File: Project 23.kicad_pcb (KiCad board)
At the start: 2 copper layers, 62 x 42 mm, 47 parts, among them J11 SRX 1, J12 SRX 2, J13 SWD, J21 Batt, J61 USB_Micro, M2 Hole_M2, Q51 Si2315, SW11 UI_Btn, SW12 PWR_BTN, U1 STM32F103C8T7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

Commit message: Completed V0.7 PCB Design
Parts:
- removed 1, M2: Hole_M2, MountingHole:MountingHole_2.2mm_M2
- removed Q51: Si2315, Package_TO_SOT_SMD:SOT-23_Handsoldering
- removed R51, R64: 10k, Resistor_SMD:R_0805_2012Metric_Pad1.15x1.40mm_HandSolder
- removed U2: MCP73811, Package_TO_SOT_SMD:SOT-23-5_HandSoldering
- removed U3: NCP551, Package_TO_SOT_SMD:SOT-23-5_HandSoldering
- removed U4: NCP1402, Package_TO_SOT_SMD:SOT-23-5_HandSoldering
- added C33: 1uF, Capacitor_SMD:C_0805_2012Metric_Pad1.15x1.40mm_HandSolder, F.Cu at (87.4, 42.7)
- added C34: 1uF, Capacitor_SMD:C_0805_2012Metric_Pad1.15x1.40mm_HandSolder, F.Cu at (80.3, 42.7)
- added C71: 1uF, Capacitor_SMD:C_0805_2012Metric_Pad1.15x1.40mm_HandSolder, F.Cu at (91.4, 62.0)
- added D11: MMBD1205, Package_TO_SOT_SMD:SOT-23, F.Cu at (79.2, 62.0)
- added H1: M2, MountingHole:MountingHole_2.2mm_M2, F.Cu at (55.8, 42.0)
- added H2: M2, MountingHole:MountingHole_2.2mm_M2, F.Cu at (64.0, 79.5)
- added H3: M2, MountingHole:MountingHole_2.2mm_M2, F.Cu at (107.8, 79.2)
- added H4: M2, MountingHole:MountingHole_2.2mm_M2, F.Cu at (107.8, 45.5)
- added J22: BATT-, Connector_PinHeader_2.54mm:PinHeader_1x01_P2.54mm_Vertical, F.Cu at (59.7, 41.9)
- added J71: Micro_SD_Card_Det, Project 23:micro sd holder, F.Cu at (108.0, 61.0)
- added R15: 10k, Resistor_SMD:R_0805_2012Metric_Pad1.15x1.40mm_HandSolder, F.Cu at (80.3, 66.3)
- added R16: 10k, Resistor_SMD:R_0805_2012Metric_Pad1.15x1.40mm_HandSolder, F.Cu at (78.2, 66.3)
- added R21: 10k, Resistor_SMD:R_0805_2012Metric_Pad1.15x1.40mm_HandSolder, F.Cu at (55.4, 47.8)
- added R22: 10k, Resistor_SMD:R_0805_2012Metric_Pad1.15x1.40mm_HandSolder, F.Cu at (62.5, 45.2)
- added R81: 10k, Resistor_SMD:R_0805_2012Metric_Pad1.15x1.40mm_HandSolder, F.Cu at (59.2, 49.0)
- added R82: 10k, Resistor_SMD:R_0805_2012Metric_Pad1.15x1.40mm_HandSolder, F.Cu at (61.2, 49.0)
- added R83: 10k, Resistor_SMD:R_0805_2012Metric_Pad1.15x1.40mm_HandSolder, F.Cu at (65.3, 49.0)
- added R84: 10k, Resistor_SMD:R_0805_2012Metric_Pad1.15x1.40mm_HandSolder, F.Cu at (63.2, 49.0)
- added TP31: 3V3SB, TestPoint:TestPoint_Pad_D2.0mm, F.Cu at (79.8, 80.2)
- added TP32: 3V3, TestPoint:TestPoint_Pad_D2.0mm, F.Cu at (77.0, 80.2)
- added TP41: 5V, TestPoint:TestPoint_Pad_D2.0mm, F.Cu at (82.5, 80.2)
- added TP75: GND, TestPoint:TestPoint_Pad_D2.0mm, F.Cu at (85.2, 80.0)
- added U21: MCP73832, Package_TO_SOT_SMD:SOT-23-5_HandSoldering, F.Cu at (55.4, 45.2)
- added U31: NCP551, Package_TO_SOT_SMD:SOT-23-5_HandSoldering, F.Cu at (83.8, 46.7)
- added U32: MIC5504, Package_TO_SOT_SMD:SOT-23-5_HandSoldering, F.Cu at (83.8, 42.7)
- added U41: NCP1402, Package_TO_SOT_SMD:SOT-23-5_HandSoldering, F.Cu at (87.2, 71.4)
- J21: value Batt -> BATT +; footprint Connector_PinHeader_2.54mm:PinHeader_1x02_P2.54mm_Vertical -> Connector_PinHeader_2.54mm:PinHeader_1x01_P2.54mm_Vertical
- J61: footprint Project 23:usbMicro -> Project 23:microUsbSunken
- moved C31 32.1 mm to (87.4, 46.7), turned to 270 degrees
- moved C32 24.3 mm to (80.3, 46.7), turned to 90 degrees
- moved C16 19.3 mm to (70.1, 47.2), turned to 0 degrees
- moved C41 16.8 mm to (79.5, 71.0)
- moved RN1 15.6 mm to (83.8, 63.2), turned to 0 degrees
- moved C19 14.6 mm to (75.9, 58.9), turned to 270 degrees
- moved C42 11.3 mm to (93.3, 76.8), turned to 270 degrees
- moved L41 9.51 mm to (82.8, 70.9)
- moved F12 9.04 mm to (78.0, 74.5), turned to 0 degrees
- moved C11 8.35 mm to (84.1, 54.9), turned to 270 degrees
- moved R63 8.19 mm to (60.7, 57.5), turned to 180 degrees
- moved U1 7.93 mm to (71.8, 53.6)
- moved C21 7.47 mm to (58.9, 45.2), turned to 90 degrees
- moved C18 7.37 mm to (66.3, 57.9), turned to 180 degrees
- moved D41 7.32 mm to (88.9, 68.1), turned to 180 degrees
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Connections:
- C16 pad 1: +3V3 -> /3V3SB
- C17 pad 1: +3V3 -> /3V3SB
- C18 pad 1: +3V3 -> /3V3SB
- C19 pad 1: +3V3 -> /3V3SB
- C21 pad 1: +BATT -> VBUS
- C22 pad 1: VBUS -> +BATT
- C32 pad 1: +3V3 -> /3V3SB
- R41 pad 1: /Boost_En -> /PWR_EN
- R63 pad 2: /USB_PU -> +3V3
- RN12 pad 3: (no net) -> Net-(J11-Pad6)
- RN12 pad 6: (no net) -> /Trigger
- SW11 pad 2: +3V3 -> /3V3SB
- SW12 pad 2: +3V3 -> /3V3SB
- U1 pad 18: /Boost_En -> /VBus_Mon
- U1 pad 19: /OLED_En -> /Batt_Mon
- U1 pad 21: /Fwd_LED -> /Rev_LED
- U1 pad 22: /Rev_LED -> /Pwr_LED
- U1 pad 24: +3V3 -> /3V3SB
- U1 pad 25: /Pwr_LED -> /SS2
- U1 pad 26: (no net) -> /SCK2
- U1 pad 27: (no net) -> /MISO2
- U1 pad 28: (no net) -> /MOSI2
- U1 pad 3: (no net) -> /Stat
- U1 pad 31: /VBus_Sense -> /Trigger
- U1 pad 36: +3V3 -> /3V3SB
- U1 pad 41: /USB_PU -> /R_DIV_En
- U1 pad 45: (no net) -> /PWR_En
- U1 pad 46: (no net) -> /Fwd_LED
- U1 pad 48: +3V3 -> /3V3SB
- U1 pad 9: +3V3 -> /3V3SB
- U5 pad 2: Net-(Q51-Pad3) -> +3V3
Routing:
- net /3V3SB: track 0.00 -> 122.3 mm, vias 0 -> 10
- net /Boost_En: track 39.5 -> 0.00 mm, vias 6 -> 0
- net /SCK2: track 0.00 -> 36.8 mm, vias 0 -> 2
- net /MISO2: track 0.00 -> 35.4 mm, vias 0 -> 2
- net /MOSI2: track 0.00 -> 35.2 mm, vias 0 -> 2
- net /SS2: track 0.00 -> 34.9 mm, vias 0 -> 2
- net /Stat: track 0.00 -> 33.1 mm, vias 0 -> 4
- net /PWR_En: track 0.00 -> 26.3 mm, vias 0 -> 4
- net GND: track 110.7 -> 86.0 mm, vias 47 -> 37
- net VBUS: track 55.0 -> 35.1 mm, vias 0 -> 2
- net /Trigger: track 0.00 -> 19.7 mm, vias 0 -> 4
- net /OLED_En: track 19.5 -> 0.00 mm
- net /R_DIV_En: track 0.00 -> 19.3 mm
- net /Batt_Mon: track 0.00 -> 16.7 mm, vias 0 -> 4
- net /Fwd_LED: track 30.2 -> 15.4 mm, vias 2 -> 0
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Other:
- outline, holes or cut-outs redrawn
- board text removed: "Goldfish Electronics"
- board text removed: "Project 23 Rev 0.6"

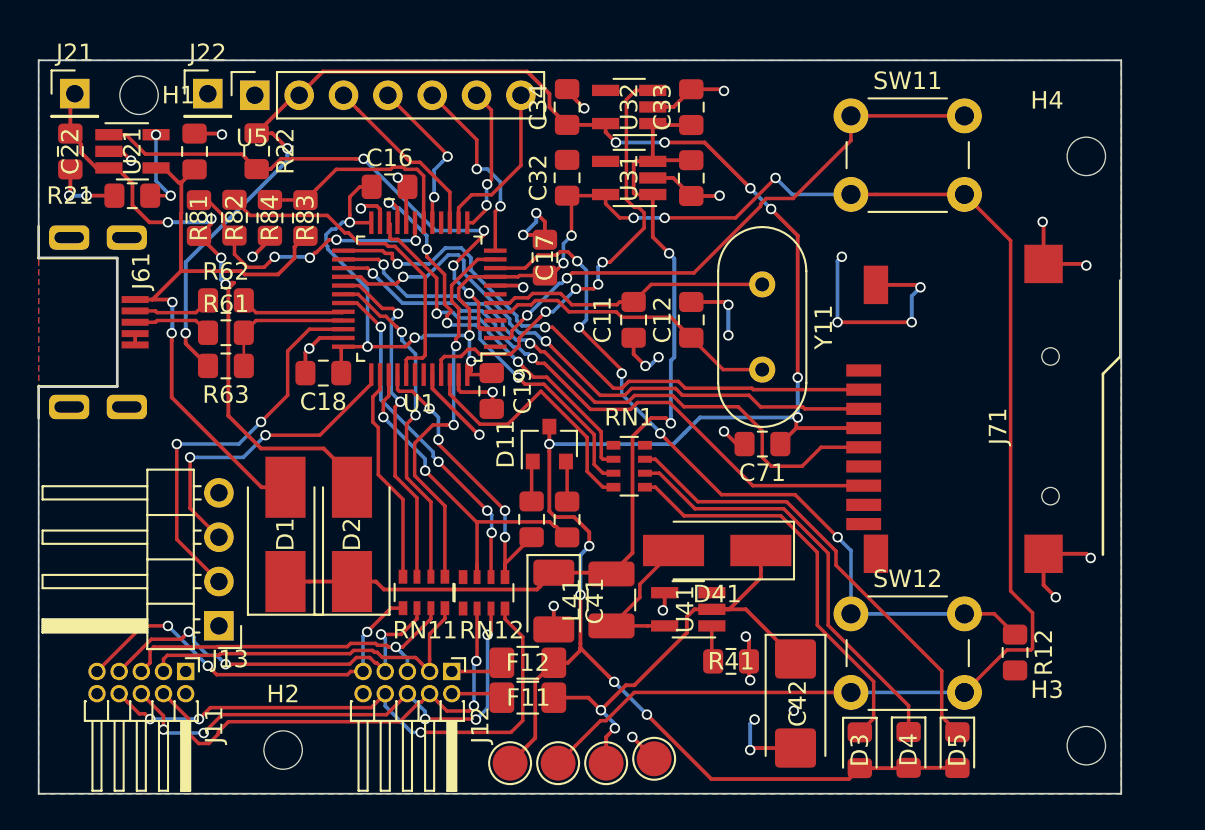
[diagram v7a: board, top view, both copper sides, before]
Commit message: Final prototype v0.7
Added logo, replaced NCP1402 as it is EOL.
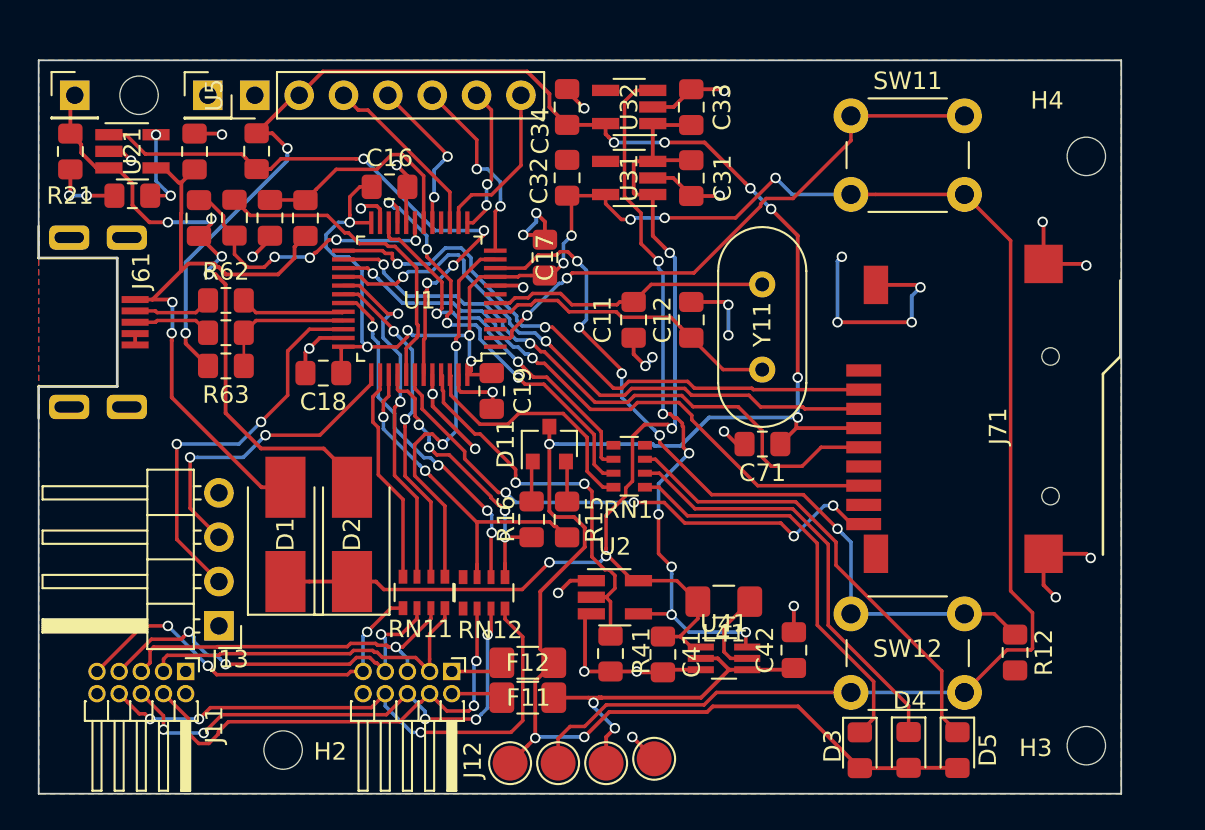
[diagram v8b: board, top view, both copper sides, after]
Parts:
- removed D41: MBRS140, Diode_SMD:D_SMA_Handsoldering
- added U2: 74AHCT1G125, Package_TO_SOT_SMD:SOT-23-5_HandSoldering, F.Cu at (83.0, 70.8)
- C41: value 10uF,Tan -> 10uF; footprint Capacitor_Tantalum_SMD:CP_EIA-3528-21_Kemet-B_Pad1.50x2.35mm_HandSolder -> Capacitor_SMD:C_0805_2012Metric_Pad1.15x1.40mm_HandSolder
- C42: value 47uF,Tan -> 10uF; footprint Capacitor_Tantalum_SMD:CP_EIA-6032-28_Kemet-C_Pad2.25x2.35mm_HandSolder -> Capacitor_SMD:C_0805_2012Metric_Pad1.15x1.40mm_HandSolder
- L41: value 47uH -> 4.7uH; footprint Inductor_SMD:L_1210_3225Metric_Pad1.42x2.65mm_HandSolder -> Inductor_SMD:L_1206_3216Metric_Pad1.42x1.75mm_HandSolder
- R21: value 10k -> 5K1
- U41: value NCP1402 -> TPS6122x; footprint Package_TO_SOT_SMD:SOT-23-5_HandSoldering -> Package_TO_SOT_SMD:SOT-363_SC-70-6_Handsoldering
- U5: footprint Connector_PinSocket_2.54mm:PinSocket_1x07_P2.54mm_Vertical -> Connector_PinHeader_2.54mm:PinHeader_1x07_P2.54mm_Vertical
- moved C41 6.96 mm to (85.8, 74.0)
- moved R41 6.92 mm to (82.8, 74.0), turned to 90 degrees
- moved L41 6.43 mm to (89.2, 71.0), turned to 180 degrees
- moved U41 3.48 mm to (89.2, 74.2), turned to 0 degrees
- moved C42 3.06 mm to (93.2, 73.8), turned to 90 degrees
- moved J22 0.10 mm to (59.7, 42.0)
- moved J21 0.09 mm to (52.1, 42.0)
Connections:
- C31 pad 1: VDD -> VCC
- C33 pad 1: VDD -> VCC
- C41 pad 1: VDD -> VCC
- D1 pad 1: VDD -> VCC
- D2 pad 1: VDD -> VCC
- J71 pad 9: (no net) -> /SD_CD
- L41 pad 2: VDD -> VCC
- R41 pad 1: /PWR_EN -> GND
- R41 pad 2: GND -> Net-(R41-Pad2)
- U1 pad 3: /Stat -> (no net)
- U1 pad 42: (no net) -> /SD_CD
- U1 pad 43: (no net) -> /Stat
- U1 pad 45: /PWR_En -> Net-(R41-Pad2)
- U31 pad 1: VDD -> VCC
- U31 pad 3: VDD -> VCC
- U32 pad 1: VDD -> VCC
- U32 pad 3: /PWR_En -> /PWR_EN
- U41 pad 1: /PWR_EN -> VCC
- U41 pad 3: (no net) -> GND
- U41 pad 4: GND -> +5V
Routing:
- net VCC: track 0.00 -> 65.2 mm, vias 0 -> 4
- net VDD: track 54.7 -> 0.00 mm, vias 2 -> 0
- net /PWR_EN: track 2.06 -> 41.3 mm, vias 0 -> 7
- net /SD_CD: track 0.00 -> 31.9 mm, vias 0 -> 4
- net /PWR_En: track 26.3 -> 0.00 mm, vias 4 -> 0
- net Net-(R41-Pad2): track 0.00 -> 24.1 mm, vias 0 -> 2
- net +5V: track 26.9 -> 21.1 mm
- net GND: track 86.0 -> 91.3 mm, vias 37 -> 35
- net Net-(L41-Pad1): track 8.84 -> 4.97 mm
- net +3V3: track 133.9 -> 135.4 mm, vias 13 -> 11
- net /Stat: track 33.1 -> 34.3 mm
- net /Fwd_LED: track 15.4 -> 14.3 mm
- net /3V3SB: track 122.3 -> 123.3 mm
- net /R_DIV_En: track 19.3 -> 18.5 mm
- net /Quad_A: track 19.9 -> 20.5 mm
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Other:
- board text added: "Goldfish Electronics"
- board text added: "Project 23 HW v0.7"
